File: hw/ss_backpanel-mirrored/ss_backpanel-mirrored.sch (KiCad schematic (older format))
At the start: 18 parts, among them J101 4mm_banana_socket-LB_I4R_A-pa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, M101 Amphenol_T3437000-DIN7_panel_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, M102 Amphenol_T3437000-DIN7_panel_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, M103 Schurter-3101_0060-fuse_holde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, M104 FN283-1-06_Schaffner_AC-panel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, M105 74980104400-Wurth_RJ45-Panel_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, M106 TE-1734346-Panel_cutout, M107 CUI-UJ2_AH_1_SMT-Panel_cutout, M108 DSub9-Kycon_K22X-E9P-N-panel_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, M109 SJ-3571N_CUI_audio_jacket_pan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, M110 SMA_bulkhead_jack_Panel_cutout, M111 Molex_NanoFit-1x02-Panel_cuto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

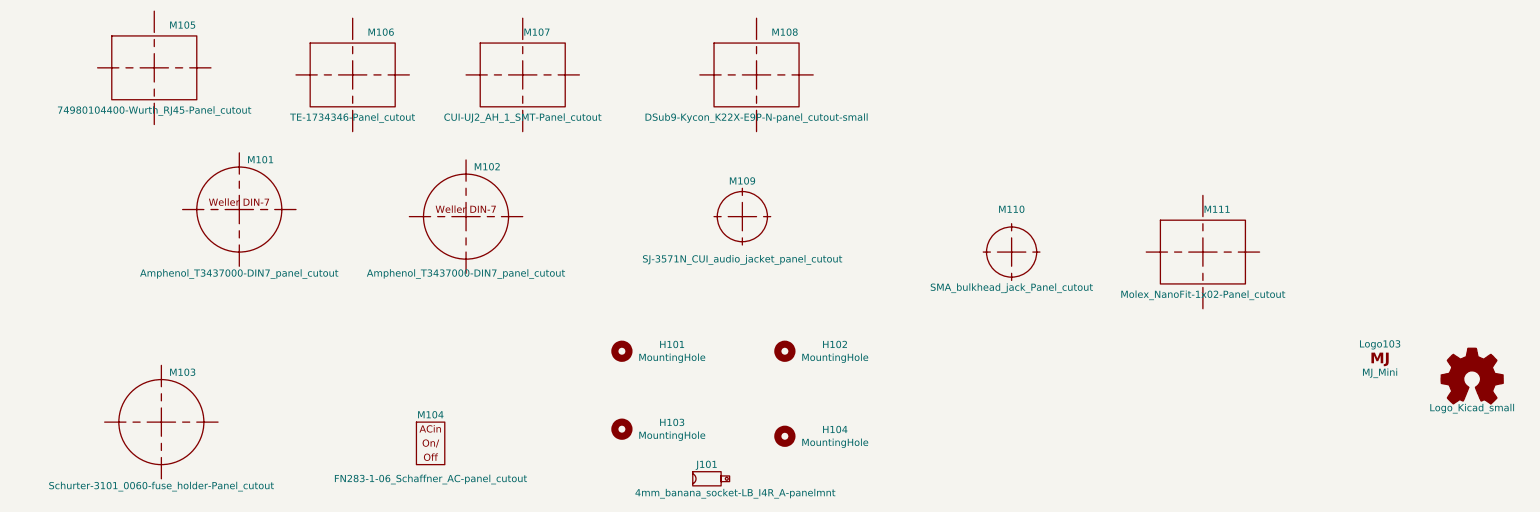
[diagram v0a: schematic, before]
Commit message: Rearpanel: IDC 2x5 instead of Dsub9 as dbg/bootstrp conn. Remove secondary fuseholder; rearrange DIN, P.E. banana, dbg. for more space. MainBoard: Rotate MW PSU 180deg (optimize for 230V through PwrBtn). PCB-fuse for 12V secondary side. IDC 2x5 instead of Dsub9; include DbgLED on free pin; ESD TVS on all dbgcon pins
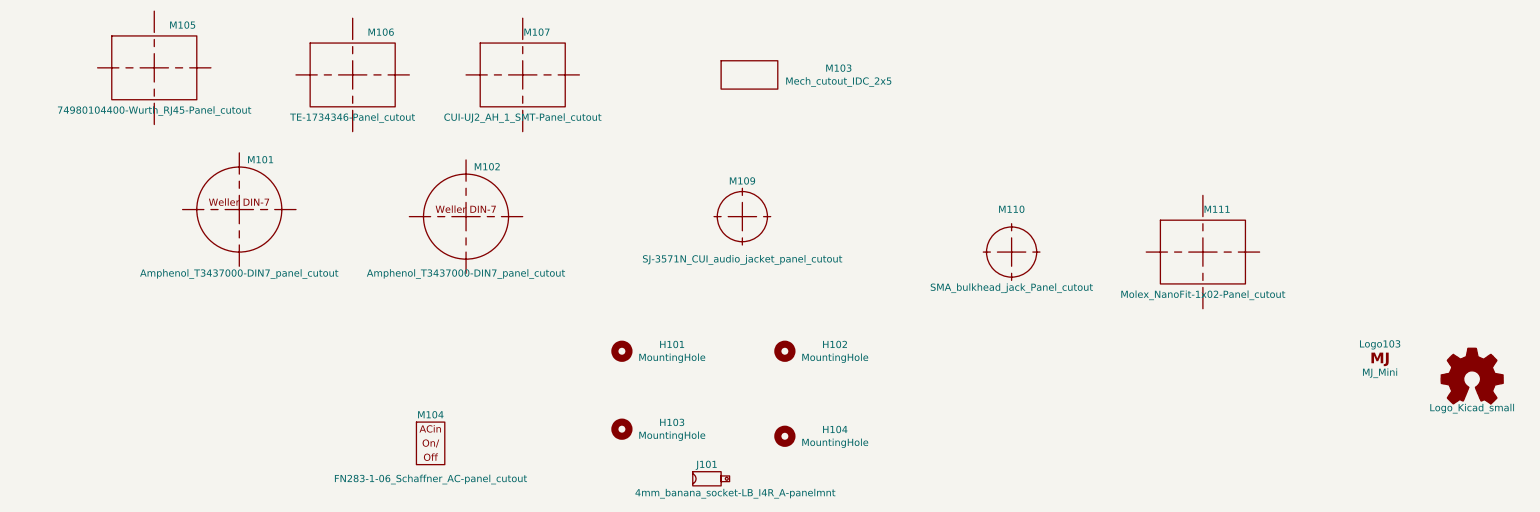
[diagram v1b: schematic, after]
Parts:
- removed M103: Schurter-3101_0060-fuse_holder-Panel_cutout, customlib_mj_fp:Schurter_3101_0060_fuse_holder-panel_cutout, symbol customlib_mj:Schurter-3101_0060-fuse_holder-Panel_cutout
- removed M108: DSub9-Kycon_K22X-E9P-N-panel_cutout-small, customlib_mj_fp:DSub9-Kycon_K22X-E9P-N_panel_cutout_behind, symbol customlib_mj:DSub9-Kycon_K22X-E9P-N-panel_cutout-small
- added M103: Mech_cutout_IDC_2x5, customlib_mj_fp:Mech_cutout_IDC_2x5, symbol customlib_mj:Mech_cutout_IDC_2x5
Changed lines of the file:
@@
-$EndComp
-$Comp
-L customlib_mj:Schurter-3101_0060-fuse_holder-Panel_cutout M103
-U 1 1 5F50285E
-P 1500 7200
-F 0 "M103" H 1650 7550 50  0000 C CNN
-F 1 "Schurter-3101_0060-fuse_holder-Panel_cutout" H 1500 6750 50  0000 C CNN
-F 2 "customlib_mj_fp:Schurter_3101_0060_fuse_holder-panel_cutout" H 1500 7200 50  0001 C CNN
-F 3 "" H 1500 7200 50  0001 C CNN
-	1    1500 7200
-	1    0    0    -1
 $EndComp
 $Comp
@@
 F 3 "" H 2850 4750 50  0001 C CNN
 	1    2850 4750
-	1    0    0    -1
-$EndComp
-$Comp
-L customlib_mj:DSub9-Kycon_K22X-E9P-N-panel_cutout-small M108
-U 1 1 5F4DCFFF
-P 5700 4750
-F 0 "M108" H 5900 5050 50  0000 C CNN
-F 1 "DSub9-Kycon_K22X-E9P-N-panel_cutout-small" H 5700 4450 50  0000 C CNN
-F 2 "customlib_mj_fp:DSub9-Kycon_K22X-E9P-N_panel_cutout_behind" H 5700 4750 50  0001 C CNN
-F 3 "" H 5700 4750 50  0001 C CNN
-	1    5700 4750
 	1    0    0    -1
 $EndComp
@@
 	1    0    0    -1
 $EndComp
+$Comp
+L customlib_mj:Mech_cutout_IDC_2x5 M103
+U 1 1 5FCE88A4
+P 5650 4750
+F 0 "M103" H 6280 4796 50  0000 C CNN
+F 1 "Mech_cutout_IDC_2x5" H 6280 4705 50  0000 C CNN
+F 2 "customlib_mj_fp:Mech_cutout_IDC_2x5" H 5650 4750 50  0001 C CNN
+F 3 "" H 5650 4750 50  0001 C CNN
+	1    5650 4750
+	1    0    0    -1
+$EndComp
